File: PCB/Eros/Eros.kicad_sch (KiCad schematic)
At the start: 97 parts, among them J1 USB_C_PowerOnly_6P, J2 UART, J3 Li-ion, J4 Conn_01x08_Socket, J6 Micro_SD_Card, Q1 BC817, SW1 SW_Push, SW2 SW_Push, SW3 SW_Push, SW4 SW_Push, SW5 SW_Push, SW6 SW_SPDT, U1 ESP32-WROOM-32E, U2 LIS3DH, U3 MCP73831-2-OT, U4 AP2112K-3.3, U5 ADS1115IDGS, U6 MCP100-315D, U7 AD8232

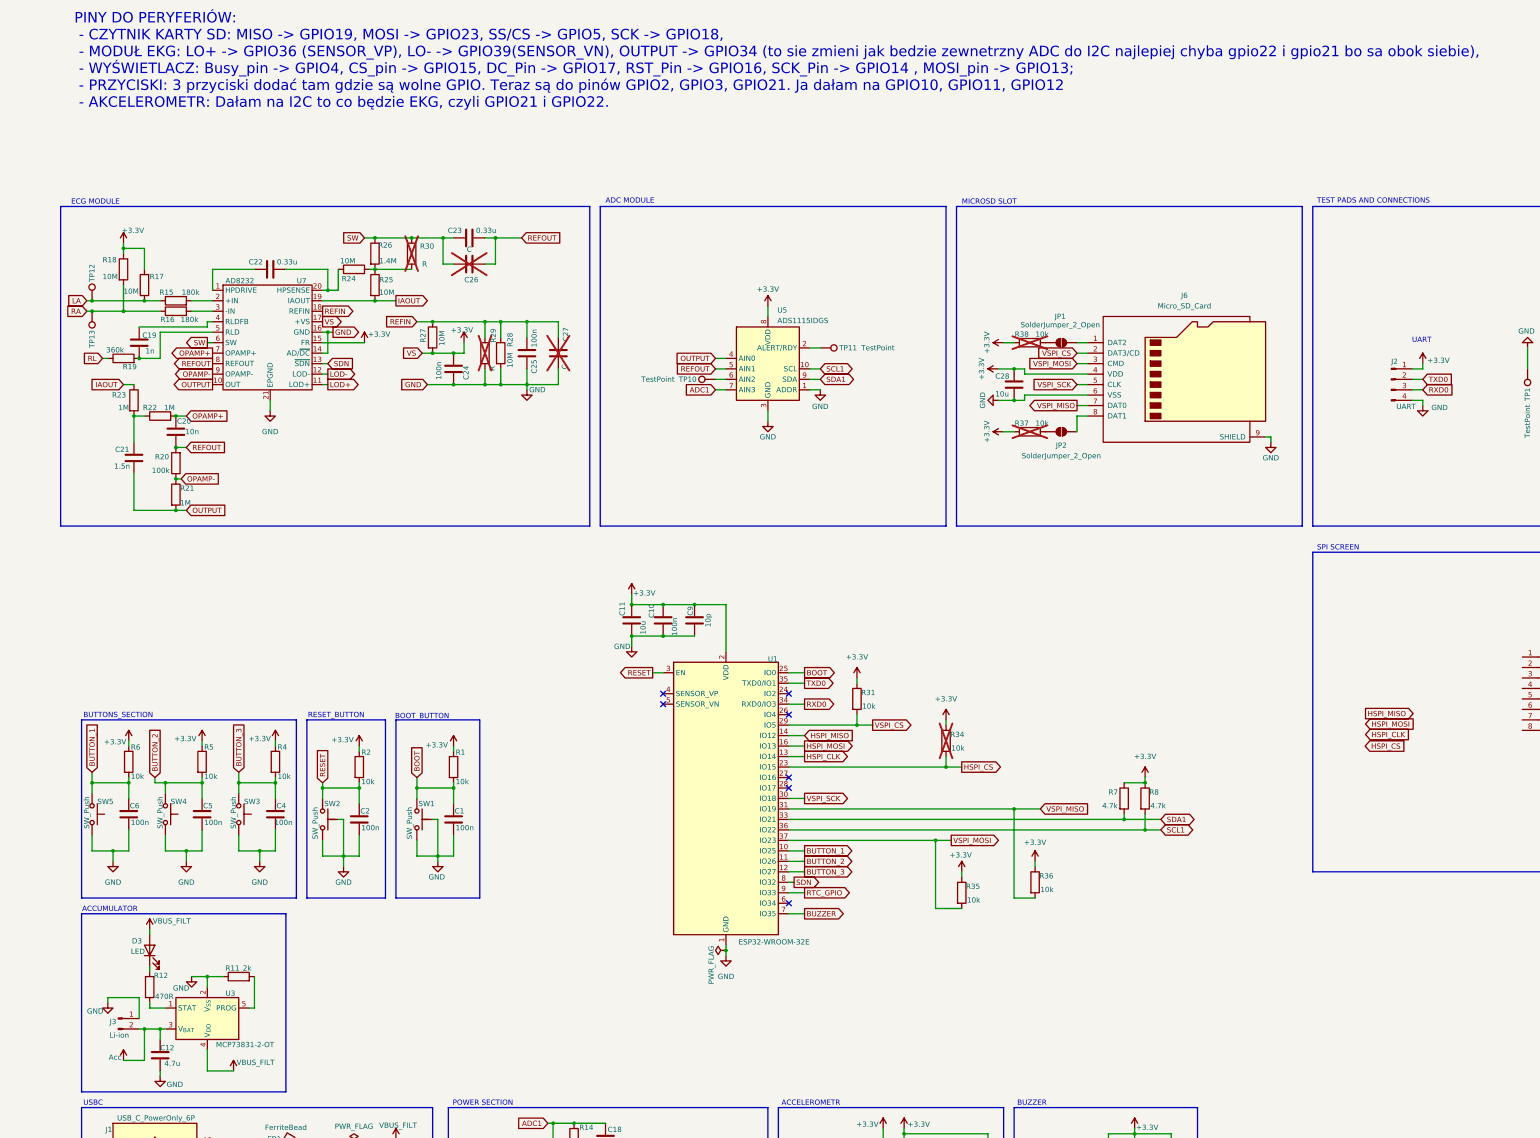
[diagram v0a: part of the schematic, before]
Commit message: add 18650 holder footprint, verify and change notes
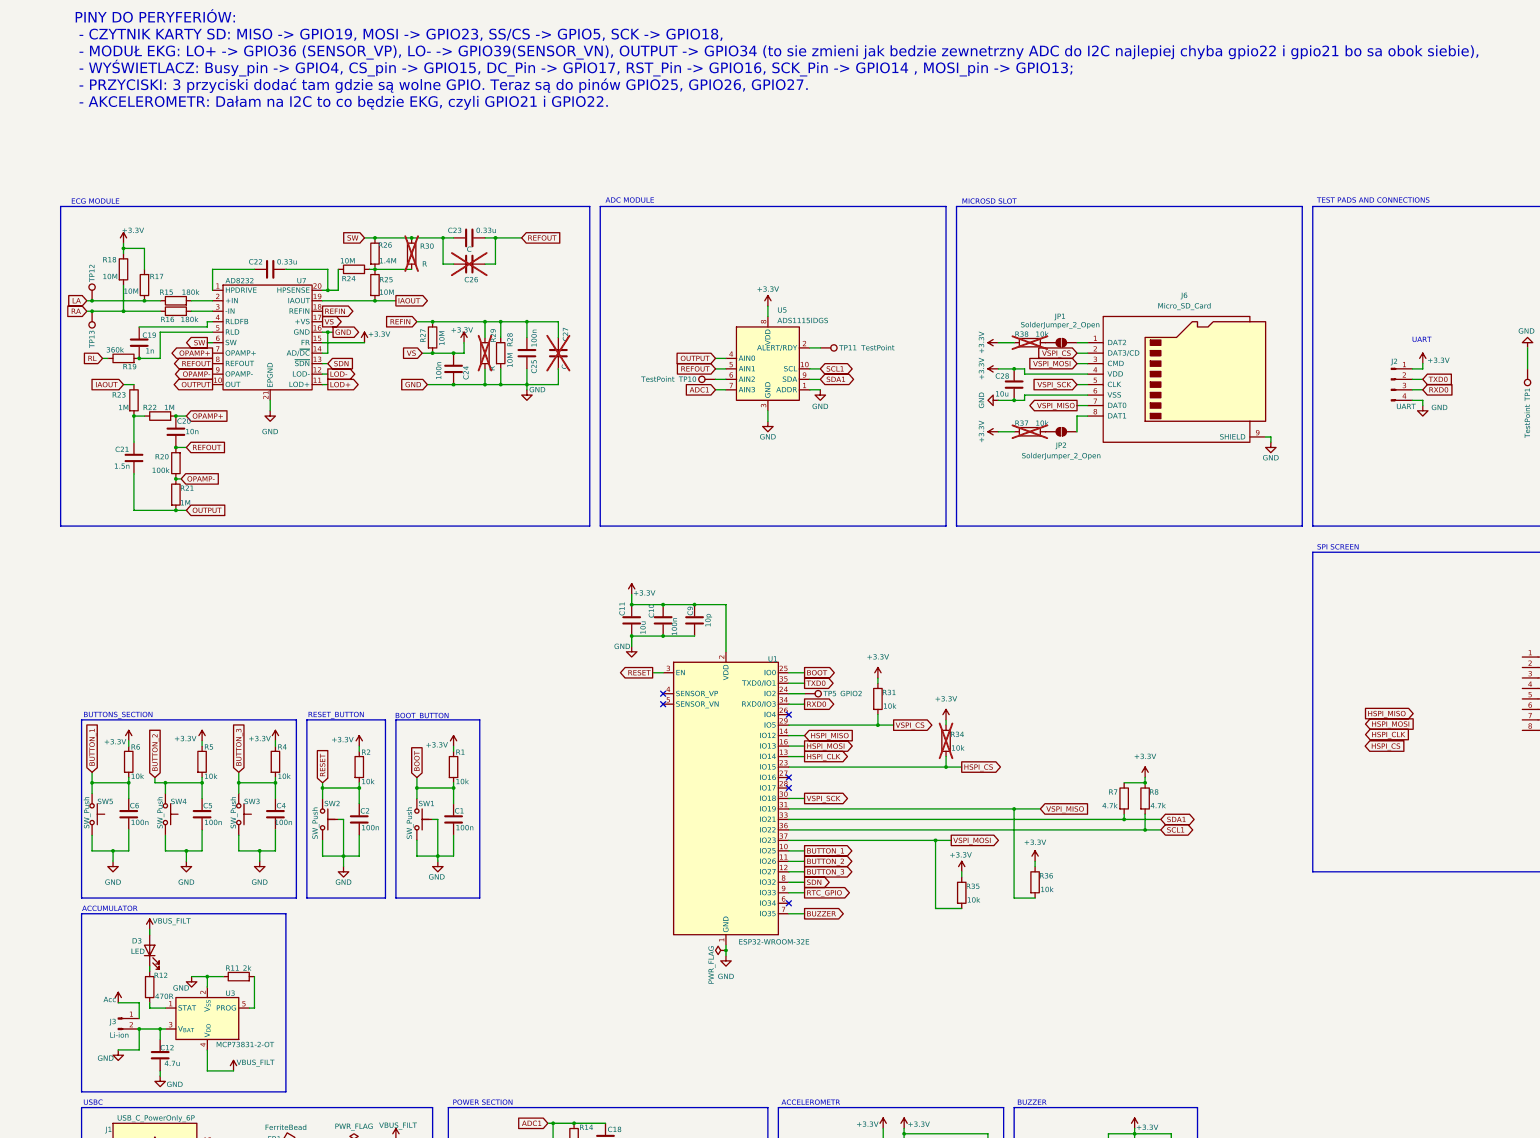
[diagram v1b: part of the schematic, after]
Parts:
- added TP5: GPIO2, TestPoint:TestPoint_Pad_D1.5mm, symbol Connector:TestPoint
- J3: footprint Connector_JST:JST_EH_S2B-EH_1x02_P2.50mm_Horizontal -> BHC-18650-1P COMF:BatteryHolder_MPD_BH-18650-PC
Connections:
- net Acc: now also J3.1 (Pin_1); no longer C12.1, J3.2 (Pin_2), U3.3 (V_{BAT})
- net GND: now also C12.1, J3.2 (Pin_2), U3.3 (V_{BAT}); no longer J3.1 (Pin_1)
- net at U1.24 (IO2): now also TP5.1
- no-connect marks 12 -> 11
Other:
- moved on the sheet: R31

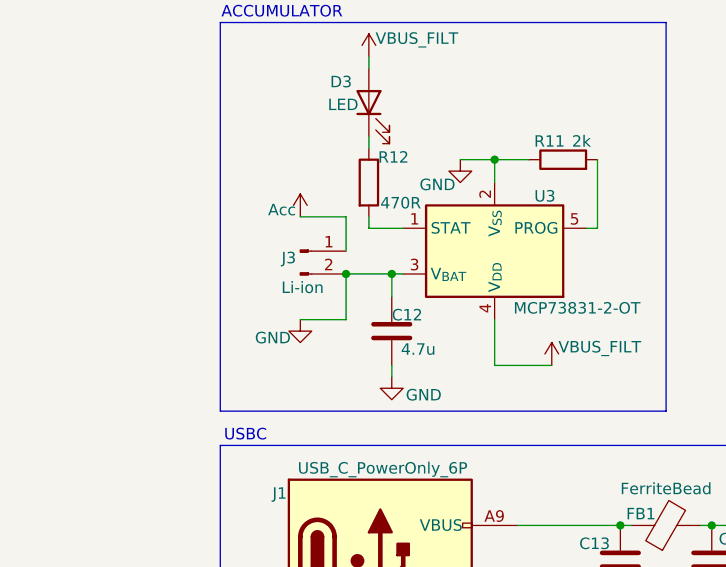
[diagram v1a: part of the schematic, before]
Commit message: flip battery
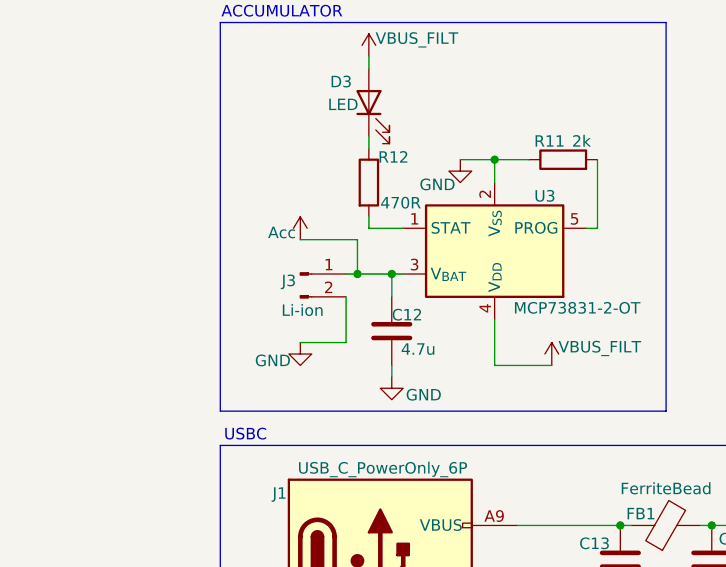
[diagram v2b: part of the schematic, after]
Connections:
- net Acc: now also C12.1, U3.3 (V_{BAT})
- net GND: no longer C12.1, U3.3 (V_{BAT})
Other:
- moved on the sheet: J3
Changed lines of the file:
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@@
 	)
 	(junction
-		(at 38.1 214.63)
-		(diameter 0)
-		(color 0 0 0 0)
-	)
-	(junction
 		(at 116.84 43.18)
 		(diameter 0)
@@
 	)
 	(junction
-		(at 33.02 214.63)
-		(diameter 0)
-		(color 0 0 0 0)
-	)
-	(junction
 		(at 231.14 260.35)
 		(diameter 0)
@@
 	)
 	(junction
+		(at 38.1 214.63)
+		(diameter 0)
+		(color 0 0 0 0)
+	)
+	(junction
 		(at 276.86 154.94)
 		(diameter 0)
@@
 	)
 	(junction
+		(at 34.29 214.63)
+		(diameter 0)
+		(color 0 0 0 0)
+	)
+	(junction
 		(at 78.74 35.56)
 		(diameter 0)
@@
 	(wire
 		(pts
+			(xy 34.29 214.63) (xy 38.1 214.63)
+		)
+		(stroke
+			(width 0)
+			(type default)
+		)
+	)
+	(wire
+		(pts
 			(xy 146.05 245.11) (xy 138.43 245.11)
 		)
@@
 	(wire
 		(pts
+			(xy 34.29 214.63) (xy 33.02 214.63)
+		)
+		(stroke
+			(width 0)
+			(type default)
+		)
+	)
+	(wire
+		(pts
 			(xy 62.23 173.99) (xy 62.23 171.45)
 		)
@@
 	(wire
 		(pts
-			(xy 33.02 219.71) (xy 33.02 214.63)
+			(xy 33.02 222.25) (xy 33.02 217.17)
 		)
 		(stroke
@@
 	(wire
 		(pts
-			(xy 27.94 219.71) (xy 33.02 219.71)
+			(xy 27.94 222.25) (xy 33.02 222.25)
 		)
 		(stroke
@@
 	(wire
 		(pts
-			(xy 33.02 208.28) (xy 27.94 208.28)
+			(xy 34.29 210.82) (xy 27.94 210.82)
 		)
 		(stroke
@@
 	(wire
 		(pts
-			(xy 33.02 214.63) (xy 38.1 214.63)
-		)
-		(stroke
-			(width 0)
-			(type default)
-		)
-	)
-	(wire
-		(pts
 			(xy 102.87 58.42) (xy 109.22 58.42)
 		)
@@
 	(wire
 		(pts
-			(xy 33.02 212.09) (xy 33.02 208.28)
+			(xy 34.29 214.63) (xy 34.29 210.82)
 		)
 		(stroke
@@
 	(symbol
 		(lib_id "power:+3.3V")
-		(at 27.94 208.28 0)
+		(at 27.94 210.82 0)
 		(unit 1)
 		(exclude_from_sim no)
@@
 		(dnp no)
 		(property "Reference" "#PWR024"
-			(at 27.94 212.09 0)
+			(at 27.94 214.63 0)
 			(effects
 				(font
@@
 		)
 		(property "Value" "Acc"
-			(at 25.908 207.518 0)
+			(at 25.908 210.058 0)
 			(effects
 				(font
@@
 		)
 		(property "Footprint" ""
-			(at 27.94 208.28 0)
+			(at 27.94 210.82 0)
 			(effects
 				(font
@@
 		)
 		(property "Datasheet" ""
-			(at 27.94 208.28 0)
+			(at 27.94 210.82 0)
 			(effects
 				(font
@@
 		)
 		(property "Description" "Power symbol creates a global label with name \"+3.3V\""
-			(at 27.94 208.28 0)
+			(at 27.94 210.82 0)
 			(effects
 				(font
@@
 	(symbol
 		(lib_id "Connector:Conn_01x02_Pin")
-		(at 27.94 212.09 0)
+		(at 27.94 214.63 0)
 		(unit 1)
 		(exclude_from_sim no)
@@
 		(dnp no)
 		(property "Reference" "J3"
-			(at 26.67 212.852 0)
+			(at 26.67 215.392 0)
 			(effects
 				(font
@@
 		)
 		(property "Value" "Li-ion"
-			(at 28.194 216.154 0)
+			(at 28.194 218.694 0)
 			(effects
 				(font
@@
 		)
 		(property "Footprint" "BHC-18650-1P COMF:BatteryHolder_MPD_BH-18650-PC"
-			(at 27.94 212.09 0)
+			(at 27.94 214.63 0)
 			(effects
 				(font
@@
 		)
 		(property "Datasheet" "~"
-			(at 27.94 212.09 0)
+			(at 27.94 214.63 0)
 			(effects
 				(font
@@
 		)
 		(property "Description" "Generic connector, single row, 01x02, script generated"
-			(at 27.94 212.09 0)
+			(at 27.94 214.63 0)
 			(effects
 				(font
@@
 	(symbol
 		(lib_id "power:GND")
-		(at 27.94 219.71 0)
+		(at 27.94 222.25 0)
 		(unit 1)
 		(exclude_from_sim no)
@@
 		(dnp no)
 		(property "Reference" "#PWR025"
-			(at 27.94 226.06 0)
+			(at 27.94 228.6 0)
 			(effects
 				(font
@@
 		)
 		(property "Value" "GND"
-			(at 24.892 221.742 0)
+			(at 24.892 224.282 0)
 			(effects
 				(font
@@
 		)
 		(property "Footprint" ""
-			(at 27.94 219.71 0)
+			(at 27.94 222.25 0)
 			(effects
 				(font
@@
 		)
 		(property "Datasheet" ""
-			(at 27.94 219.71 0)
+			(at 27.94 222.25 0)
 			(effects
 				(font
@@
 		)
 		(property "Description" "Power symbol creates a global label with name \"GND\" , ground"
-			(at 27.94 219.71 0)
+			(at 27.94 222.25 0)
 			(effects
 				(font

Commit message: wire waveshare Waveshare 12955 e-ink
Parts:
- added TP6: TestPoint, TestPoint:TestPoint_Pad_D1.5mm, symbol Connector:TestPoint
- J4: footprint LED_SMD:LED_0402_1005Metric_Pad0.77x0.64mm_HandSolder -> Connector_JST:JST_PH_S8B-PH-K_1x08_P2.00mm_Horizontal
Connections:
- net +3.3V: now also J4.1 (Pin_1)
- net GND: now also J4.2 (Pin_2)
- net HSPI_CLK: now also J4.4 (Pin_4)
- net HSPI_CS: now also J4.5 (Pin_5)
- net HSPI_MISO: now also TP6.1
- net HSPI_MOSI: now also J4.3 (Pin_3)
- net DISP_DC: now reaches J4.6 (Pin_6)
- net DISP_DC: now also U1.28 (IO17)
- net DISP_RST: now reaches J4.7 (Pin_7)
- net DISP_RST: now also U1.27 (IO16)
- net DISP_BUSY: now reaches J4.8 (Pin_8)
- net DISP_BUSY: now also U1.26 (IO4)
- no-connect marks 11 -> 8
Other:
- note added: "power supply supervisor i bms"
- note removed: "Jula dodaj power supply supervisor i poczytaj o bms (baterry management systems)!!! ZROBIŁAM"

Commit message: connect LOD+/-, add pinHeader for RA LA RL
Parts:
- removed TP12, TP13, TP6: TestPoint, TestPoint:TestPoint_Pad_D1.5mm, symbol Connector:TestPoint
- added J5: Conn_01x03_Socket, Connector_PinSocket_2.54mm:PinSocket_1x03_P2.54mm_Vertical, symbol Connector:Conn_01x03_Socket
- added JP3: SolderJumper_2_Open, Jumper:SolderJumper-2_P1.3mm_Open_Pad1.0x1.5mm, symbol Jumper:SolderJumper_2_Open
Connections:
- net HSPI_MISO is gone; now on net LOD+: U1.14 (IO12)
- net LA: now also J5.2 (Pin_2)
- net LOD-: now also U1.6 (IO34)
- net OUTPUT: now also JP3.1 (A)
- net RA: now also J5.1 (Pin_1)
- net RL: now also J5.3 (Pin_3)
- net at U1.4 (SENSOR_VP): now also JP3.2 (B)
- no-connect marks 8 -> 6
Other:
- note added: "PINY DO PERYFERIÓW: - CZYTNIK KARTY SD: MISO -> GPIO19, MOSI -> GPIO23, SS/CS -> GPIO5, SCK -> GPIO18, - MODUŁ EKG: OUTPUT -> ADIN0 / SENSOR_VP - WYŚWIETLACZ: Busy_pin -> GPIO4, CS_pin -> GPIO15, DC_Pin -> GPIO17, RST_Pin -> GPIO16, SCK_Pin -> GPIO14 , MOSI_pin -> GPIO13; - PRZYCISKI: 3 przyciski dodać tam gdzie są wolne GPIO. Teraz są do pinów GPIO25, GPIO26, GPIO27. - AKCELEROMETR: Dałam na I2C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"
- note removed: "PINY DO PERYFERIÓW: - CZYTNIK KARTY SD: MISO -> GPIO19, MOSI -> GPIO23, SS/CS -> GPIO5, SCK -> GPIO18, - MODUŁ EKG: LO+ -> GPIO36 (SENSOR_VP), LO- -> GPIO39(SENSOR_VN), OUTPUT -> GPIO34 (to sie zmieni jak bedzie zewnetrzny ADC do I2C najlepiej chyba gpio22 i gpio21 bo sa obok siebie), - WYŚWIETLACZ: Busy_pin -> GPIO4, CS_pin -> GPIO15, DC_Pin -> GPIO17, RST_Pin -> GPIO16, SCK_Pin -> GPIO14 , MOSI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"

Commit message: Wire OPA333
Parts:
- removed TP10: TestPoint, TestPoint:TestPoint_Pad_D1.5mm, symbol Connector:TestPoint
- added C29, C30: 100n, Capacitor_SMD:C_0402_1005Metric_Pad0.74x0.62mm_HandSolder, symbol Device:C
- added J7: AudioJack3_Ground, Connector_Audio:Jack_3.5mm_Lumberg_1503_03_Horizontal, symbol Connector_Audio:AudioJack3_Ground
- added JP4: SolderJumper_2_Open, Jumper:SolderJumper-2_P1.3mm_Open_Pad1.0x1.5mm, symbol Jumper:SolderJumper_2_Open
- added R32: 10k, Resistor_SMD:R_0402_1005Metric_Pad0.72x0.64mm_HandSolder, symbol Device:R
- added U8: OPA333xxD, Package_SO:SOIC-8_3.9x4.9mm_P1.27mm, symbol Amplifier_Operational:OPA333xxD
- J5: footprint Connector_PinSocket_2.54mm:PinSocket_1x03_P2.54mm_Vertical -> Connector_PinHeader_1.27mm:PinHeader_1x03_P1.27mm_Vertical
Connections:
- net +3.3V: now also C29.1, U8.7 (V+)
- net GND: now also C29.2, C30.2, J7.G, U8.4 (V-)
- net LA: now also J7.R
- net OUTPUT: now also JP4.1 (A), R32.1; no longer U5.4 (AIN0)
- net RA: now also J7.S
- net RL: now also J7.T
- net at U5.6 (AIN2): now also JP4.2 (B)
- new net: C30.1, R32.2, U8.3 (+)
- new net OUTPUT_BUFFER: U5.4 (AIN0), U8.2 (-), U8.6
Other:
- moved on the sheet: C28, J2, J4, J5, J6, JP1, JP2, R37, R38, TP1, TP2, TP3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

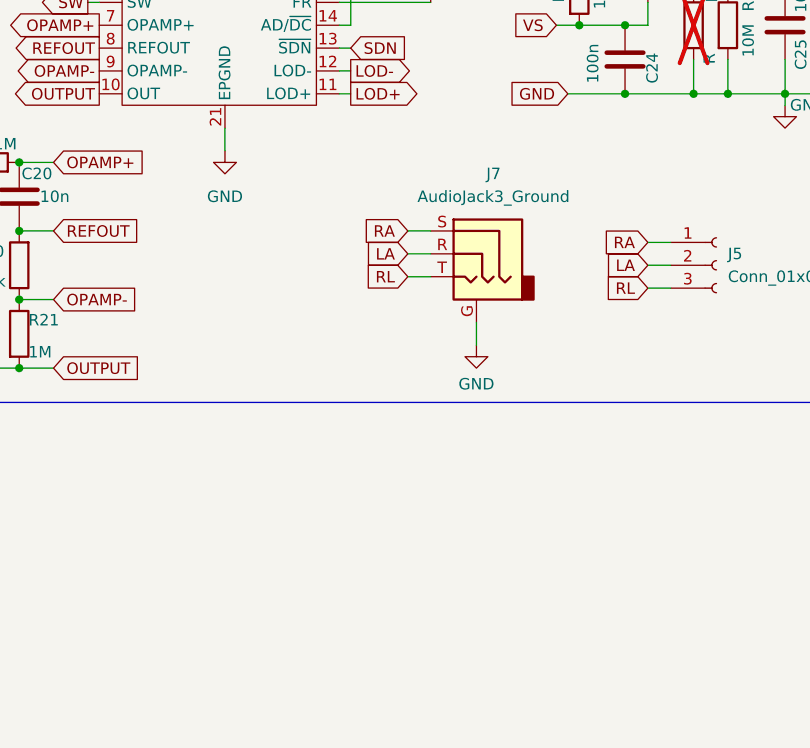
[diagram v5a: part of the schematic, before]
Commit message: Wstępne rozmieszczenie brzegowych elementów
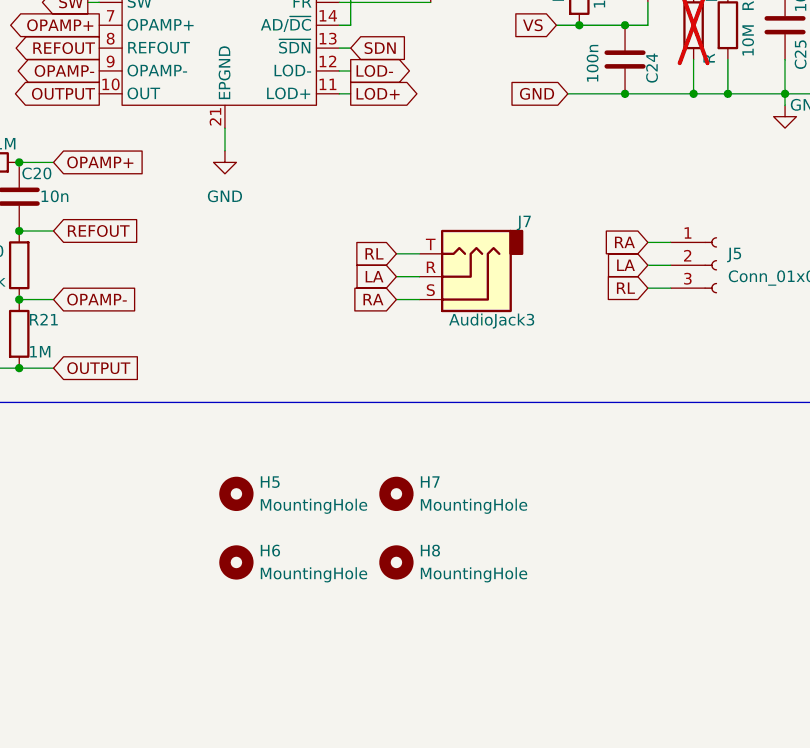
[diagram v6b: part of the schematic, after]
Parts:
- removed J7: AudioJack3_Ground, Connector_Audio:Jack_3.5mm_Lumberg_1503_03_Horizontal, symbol Connector_Audio:AudioJack3_Ground
- added H5, H6, H7, H8: MountingHole, MountingHole:MountingHole_3.2mm_M3_Pad, symbol Mechanical:MountingHole
- added J7: AudioJack3, Connector_Audio:Jack_3.5mm_Lumberg_1503_03_Horizontal, symbol Connector_Audio:AudioJack3
- J4: footprint Connector_JST:JST_PH_S8B-PH-K_1x08_P2.00mm_Horizontal -> Connector_JST:JST_PH_B8B-PH-K_1x08_P2.00mm_Vertical
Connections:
- net LA: now also J7.R
- net RA: now also J7.S
- net RL: now also J7.T

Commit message: Wstępne ułożenie komponentów
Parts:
- R13, R14: value 100k -> 1M
- renumbered TP11 to TP6
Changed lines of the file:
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@@
 		(on_board yes)
 		(dnp no)
-		(property "Reference" "TP11"
+		(property "Reference" "TP6"
 			(at 202.692 49.53 90)
 			(effects
@@
 			(project "Eros"
 				(path "/0de1f6b5-5206-4036-b96d-057d224718dc"
-					(reference "TP11")
+					(reference "TP6")
 					(unit 1)
 				)
@@
 			)
 		)
-		(property "Value" "100k"
+		(property "Value" "1M"
 			(at 127.254 249.428 0)
 			(effects
@@
 			)
 		)
-		(property "Value" "100k"
+		(property "Value" "1M"
 			(at 139.7 243.332 0)
 			(effects
